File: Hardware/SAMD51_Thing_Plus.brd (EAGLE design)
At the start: 22.9 x 50.8 mm, 107 parts, among them J6 AMP FCI 10103594-0001LF, Q1 2.5A/30V, U1 MCP73831, U2 ATSAMD51J20A-A, U3 AP2112K-3.3V, U4 4MB Flash, Y1 32.768kHz

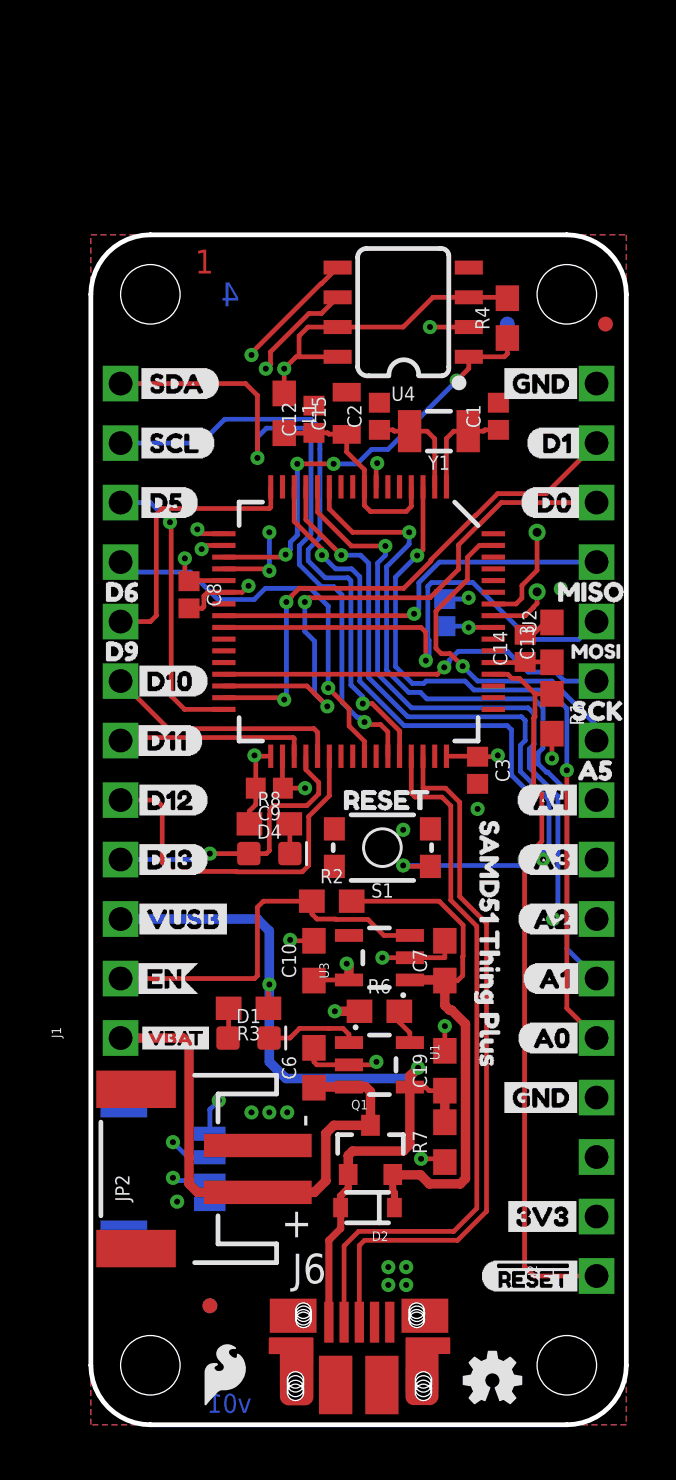
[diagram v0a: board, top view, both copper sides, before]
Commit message: Moving QWIIC connector, adding board name, moving bottom-placed capacitor to top
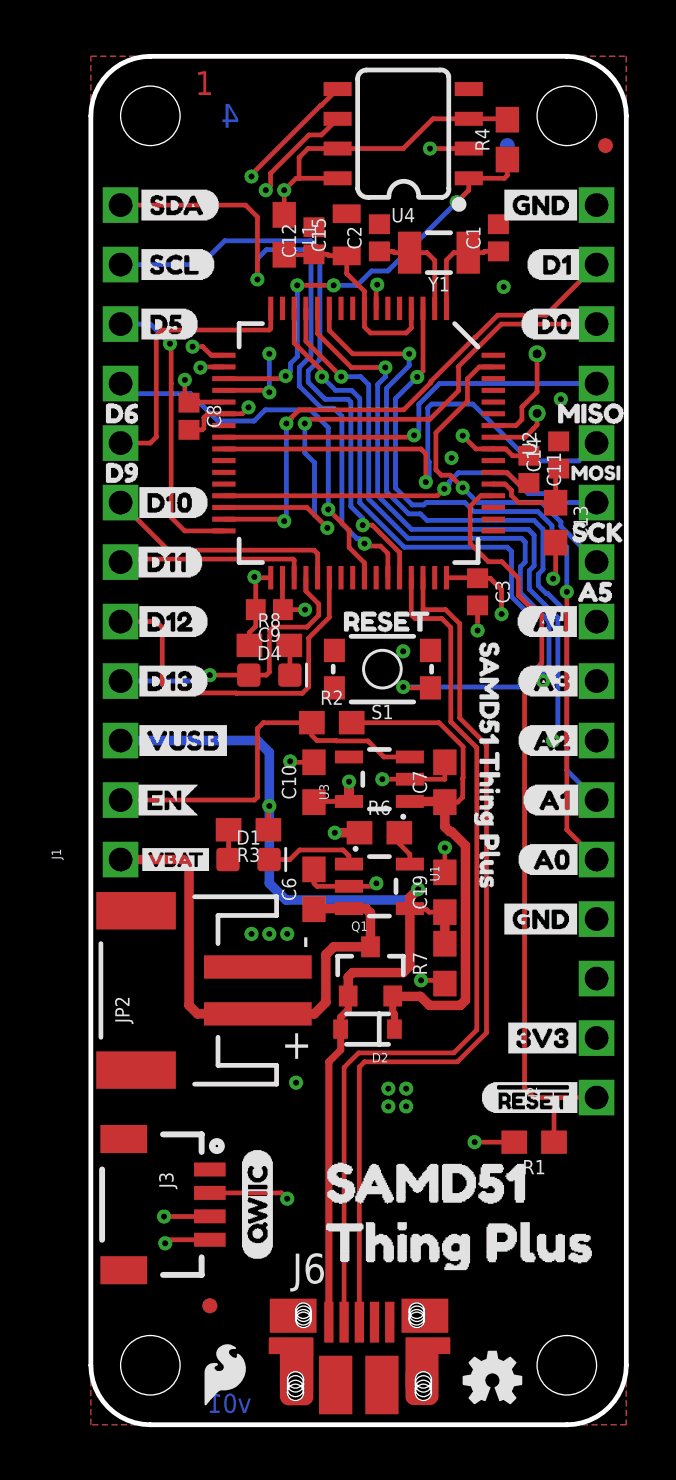
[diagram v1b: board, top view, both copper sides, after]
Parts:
- removed U$61: (no value), buzzard_labels (49):SAMD51_THING_PLUS0
- added U$63, U$65: (no value), buzzard_labels:SAMD510
- added U$64, U$66: (no value), buzzard_labels:THING_PLUS1
- moved R1 18.3 mm to (18.9, 12.1), turned to 180 degrees
- moved C14 8.38 mm to (20.0, 41.4)
- moved C1 7.62 mm to (17.4, 50.7)
- moved C2 7.62 mm to (12.3, 50.7)
- moved U$17 7.62 mm to (18.3, 47.0)
- moved U$18 7.62 mm to (18.5, 49.5)
- moved U$29 7.62 mm to (1.78, 47.0)
- moved U$30 7.62 mm to (1.78, 49.5)
- moved U$43 7.62 mm to (21.2, 44.5)
- moved U$44 7.62 mm to (21.2, 47.0)
- moved U$45 7.62 mm to (21.2, 49.5)
- moved U$48 7.62 mm to (5.97, 49.5)
- moved U$49 7.62 mm to (5.21, 47.0)
- moved U$50 7.62 mm to (5.21, 44.5)
- moved U4 7.62 mm to (13.3, 55.1)
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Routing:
- net SCL: track 55.9 -> 63.8 mm, vias 3 -> 2
- net D-: track 30.7 -> 38.3 mm
- net V_USB: track 36.6 -> 44.2 mm
- net D+: track 30.4 -> 38.0 mm
- net 3.3V: track 28.1 -> 33.3 mm
- net !RESET: track 37.5 -> 39.6 mm
- net VCC: track 2.52 -> 4.70 mm
- net GND: track 21.4 -> 23.4 mm, vias 21 -> 23
- net SDA: track 64.3 -> 62.6 mm
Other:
- board size 22.9 x 50.8 mm -> 22.9 x 58.4 mm

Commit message: updating version number
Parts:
- moved U$63 0.63 mm to (8.89, 9.53)
- moved U$64 0.63 mm to (8.89, 6.99)
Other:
- board text added: "Mike Hord and M. West"
- board text added: "v02"
- board text removed: "Mike Hord"
- board text removed: "v01"
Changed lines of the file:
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@@
 <setting verticaltext="up"/>
 </settings>
-<grid distance="0.00625" unitdist="inch" unit="inch" style="lines" multiple="1" display="yes" altdistance="0.001" altunitdist="inch" altunit="inch"/>
+<grid distance="0.0125" unitdist="inch" unit="inch" style="lines" multiple="1" display="yes" altdistance="0.005" altunitdist="inch" altunit="inch"/>
 <layers>
 <layer number="1" name="Top" color="4" fill="1" visible="yes" active="yes"/>
-<layer number="2" name="Route2" color="1" fill="3" visible="yes" active="yes"/>
-<layer number="15" name="Route15" color="4" fill="6" visible="yes" active="yes"/>
 <layer number="16" name="Bottom" color="1" fill="1" visible="yes" active="yes"/>
 <layer number="17" name="Pads" color="2" fill="1" visible="yes" active="yes"/>
@@
 <layer number="21" name="tPlace" color="16" fill="1" visible="yes" active="yes"/>
 <layer number="22" name="bPlace" color="14" fill="1" visible="yes" active="yes"/>
-<layer number="23" name="tOrigins" color="15" fill="1" visible="no" active="yes"/>
+<layer number="23" name="tOrigins" color="15" fill="1" visible="yes" active="yes"/>
 <layer number="24" name="bOrigins" color="15" fill="1" visible="yes" active="yes"/>
 <layer number="25" name="tNames" color="7" fill="1" visible="no" active="yes"/>
@@
 <layer number="31" name="tCream" color="7" fill="4" visible="no" active="yes"/>
 <layer number="32" name="bCream" color="7" fill="5" visible="no" active="yes"/>
+<layer number="33" name="tFinish" color="6" fill="3" visible="no" active="yes"/>
+<layer number="34" name="bFinish" color="6" fill="6" visible="no" active="yes"/>
+<layer number="35" name="tGlue" color="7" fill="4" visible="no" active="yes"/>
+<layer number="36" name="bGlue" color="7" fill="5" visible="no" active="yes"/>
+<layer number="37" name="tTest" color="7" fill="1" visible="no" active="yes"/>
+<layer number="38" name="bTest" color="7" fill="1" visible="no" active="yes"/>
 <layer number="39" name="tKeepout" color="4" fill="11" visible="no" active="yes"/>
-<layer number="40" name="bKeepout" color="1" fill="11" visible="yes" active="yes"/>
-<layer number="41" name="tRestrict" color="4" fill="10" visible="yes" active="yes"/>
-<layer number="42" name="bRestrict" color="1" fill="10" visible="yes" active="yes"/>
-<layer number="43" name="vRestrict" color="2" fill="10" visible="yes" active="yes"/>
+<layer number="40" name="bKeepout" color="1" fill="11" visible="no" active="yes"/>
+<layer number="41" name="tRestrict" color="4" fill="10" visible="no" active="yes"/>
+<layer number="42" name="bRestrict" color="1" fill="10" visible="no" active="yes"/>
+<layer number="43" name="vRestrict" color="2" fill="10" visible="no" active="yes"/>
 <layer number="44" name="Drills" color="7" fill="1" visible="no" active="yes"/>
-<layer number="45" name="Holes" color="7" fill="1" visible="no" active="yes"/>
+<layer number="45" name="Holes" color="7" fill="1" visible="yes" active="yes"/>
 <layer number="46" name="Milling" color="3" fill="1" visible="no" active="yes"/>
 <layer number="47" name="Measures" color="7" fill="1" visible="no" active="yes"/>
 <layer number="48" name="Document" color="7" fill="1" visible="no" active="yes"/>
 <layer number="49" name="Reference" color="7" fill="1" visible="no" active="yes"/>
-<layer number="51" name="tDocu" color="6" fill="1" visible="no" active="yes"/>
+<layer number="50" name="dxf" color="7" fill="1" visible="no" active="yes"/>
+<layer number="51" name="tDocu" color="6" fill="1" visible="yes" active="yes"/>
 <layer number="52" name="bDocu" color="7" fill="1" visible="no" active="yes"/>
+<layer number="91" name="Nets" color="2" fill="1" visible="no" active="no"/>
+<layer number="92" name="Busses" color="1" fill="1" visible="no" active="no"/>
+<layer number="93" name="Pins" color="2" fill="1" visible="no" active="no"/>
+<layer number="94" name="Symbols" color="4" fill="1" visible="no" active="no"/>
+<layer number="95" name="Names" color="7" fill="1" visible="no" active="no"/>
+<layer number="96" name="Values" color="7" fill="1" visible="no" active="no"/>
+<layer number="2" name="Route2" color="1" fill="3" visible="no" active="yes"/>
+<layer number="15" name="Route15" color="4" fill="6" visible="no" active="yes"/>
 <layer number="3" name="Route3" color="4" fill="3" visible="no" active="no"/>
 <layer number="4" name="Route4" color="1" fill="4" visible="no" active="no"/>
@@
 <layer number="13" name="Route13" color="4" fill="5" visible="no" active="no"/>
 <layer number="14" name="Route14" color="1" fill="6" visible="no" active="no"/>
-<layer number="33" name="tFinish" color="6" fill="3" visible="no" active="no"/>
-<layer number="34" name="bFinish" color="6" fill="6" visible="no" active="no"/>
-<layer number="35" name="tGlue" color="7" fill="4" visible="no" active="no"/>
-<layer number="36" name="bGlue" color="7" fill="5" visible="no" active="no"/>
-<layer number="37" name="tTest" color="7" fill="1" visible="no" active="no"/>
-<layer number="38" name="bTest" color="7" fill="1" visible="no" active="no"/>
-<layer number="50" name="dxf" color="7" fill="1" visible="no" active="no"/>
 <layer number="53" name="tGND_GNDA" color="7" fill="9" visible="no" active="no"/>
 <layer number="54" name="bGND_GNDA" color="1" fill="9" visible="no" active="no"/>
@@
 <layer number="89" name="SimProbes" color="9" fill="1" visible="no" active="no"/>
 <layer number="90" name="Modules" color="5" fill="1" visible="no" active="no"/>
-<layer number="91" name="Nets" color="2" fill="1" visible="no" active="no"/>
-<layer number="92" name="Busses" color="1" fill="1" visible="no" active="no"/>
-<layer number="93" name="Pins" color="2" fill="1" visible="no" active="no"/>
-<layer number="94" name="Symbols" color="4" fill="1" visible="no" active="no"/>
-<layer number="95" name="Names" color="7" fill="1" visible="no" active="no"/>
-<layer number="96" name="Values" color="7" fill="1" visible="no" active="no"/>
 <layer number="97" name="Info" color="7" fill="1" visible="no" active="no"/>
 <layer number="98" name="Guide" color="6" fill="1" visible="no" active="no"/>
@@
 <board>
 <plain>
-<text x="13.97" y="-19.05" size="1.778" layer="51" font="vector" ratio="15">Mike Hord</text>
+<text x="13.97" y="-19.05" size="1.778" layer="51" font="vector" ratio="15">Mike Hord and M. West</text>
 <text x="26.67" y="1.27" size="1.778" layer="47" font="vector" ratio="15">Units in inches</text>
 <wire x1="2.54" y1="58.42" x2="20.32" y2="58.42" width="0.2032" layer="20"/>
@@
 <text x="4.445" y="55.372" size="1.016" layer="15" font="vector" ratio="20">3</text>
 <text x="6.35" y="55.372" size="1.016" layer="16" font="vector" ratio="20" rot="MR0">4</text>
-<text x="6.858" y="0.508" size="0.8128" layer="16" font="vector" ratio="25" rot="MR0">v01</text>
+<text x="6.858" y="0.508" size="0.8128" layer="16" font="vector" ratio="25" rot="MR0">v02</text>
 <dimension x1="0" y1="58.42" x2="0" y2="0" x3="-13.97" y3="29.21" textsize="1.27" textratio="15" layer="47" dtype="vertical" unit="inch"/>
 <dimension x1="2.54" y1="55.88" x2="0" y2="0" x3="-11.43" y3="27.94" textsize="1.27" textratio="15" layer="47" dtype="vertical" unit="inch"/>
@@
 <element name="U$62" library="buzzard_labels (46)" package="QWIIC26" value="" x="7.112" y="6.985" rot="R90"/>
 <element name="U$60" library="buzzard_labels (50)" package="SAMD51_THING_PLUS0" value="" x="17.018" y="34.163" rot="R270"/>
-<element name="U$63" library="buzzard_labels" package="SAMD510" value="" x="8.89" y="10.16"/>
-<element name="U$64" library="buzzard_labels" package="THING_PLUS1" value="" x="8.89" y="7.62"/>
+<element name="U$63" library="buzzard_labels" package="SAMD510" value="" x="8.89" y="9.525"/>
+<element name="U$64" library="buzzard_labels" package="THING_PLUS1" value="" x="8.89" y="6.985"/>
 <element name="U$65" library="buzzard_labels" package="SAMD510" value="" x="23.01875" y="9.2075" rot="MR0"/>
 <element name="U$66" library="buzzard_labels" package="THING_PLUS1" value="" x="13.49375" y="9.36625" rot="MR0"/>

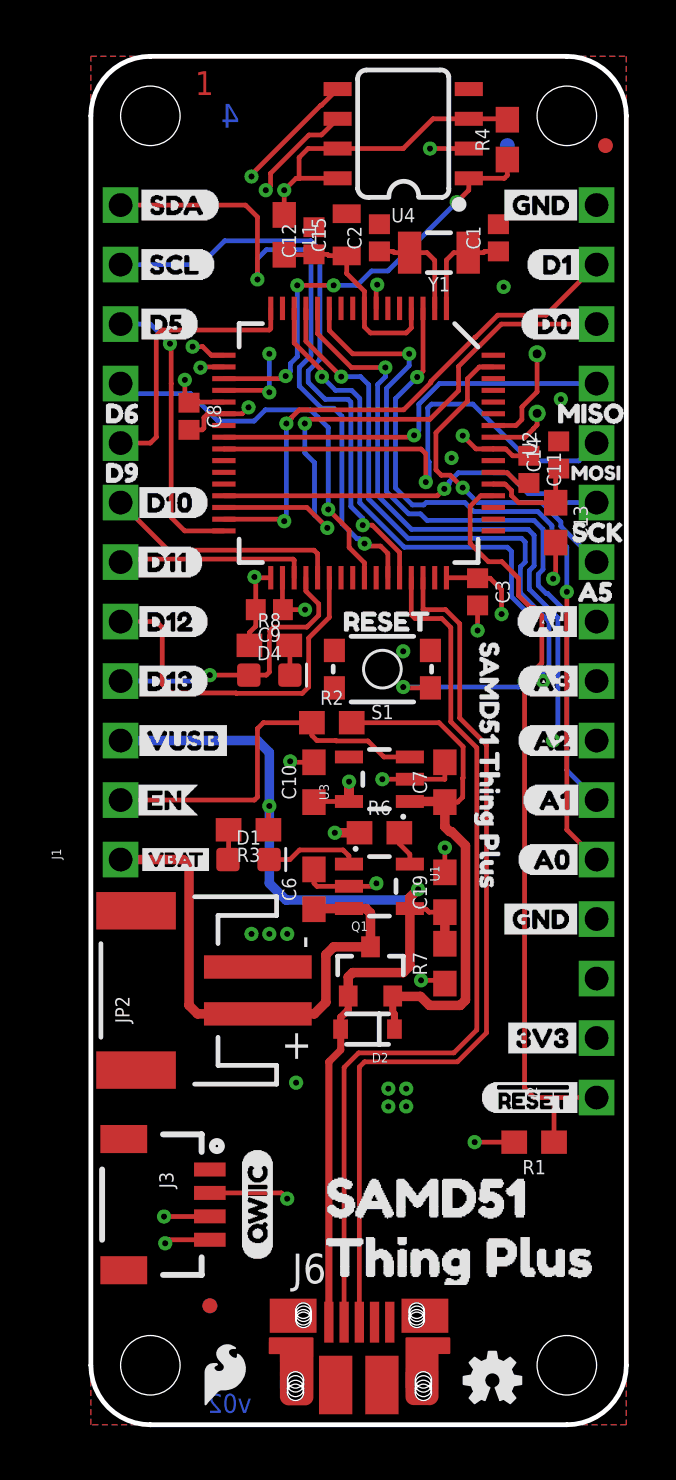
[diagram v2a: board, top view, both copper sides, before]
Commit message: connecting D4 to match feather footprint, removing short on USB connector
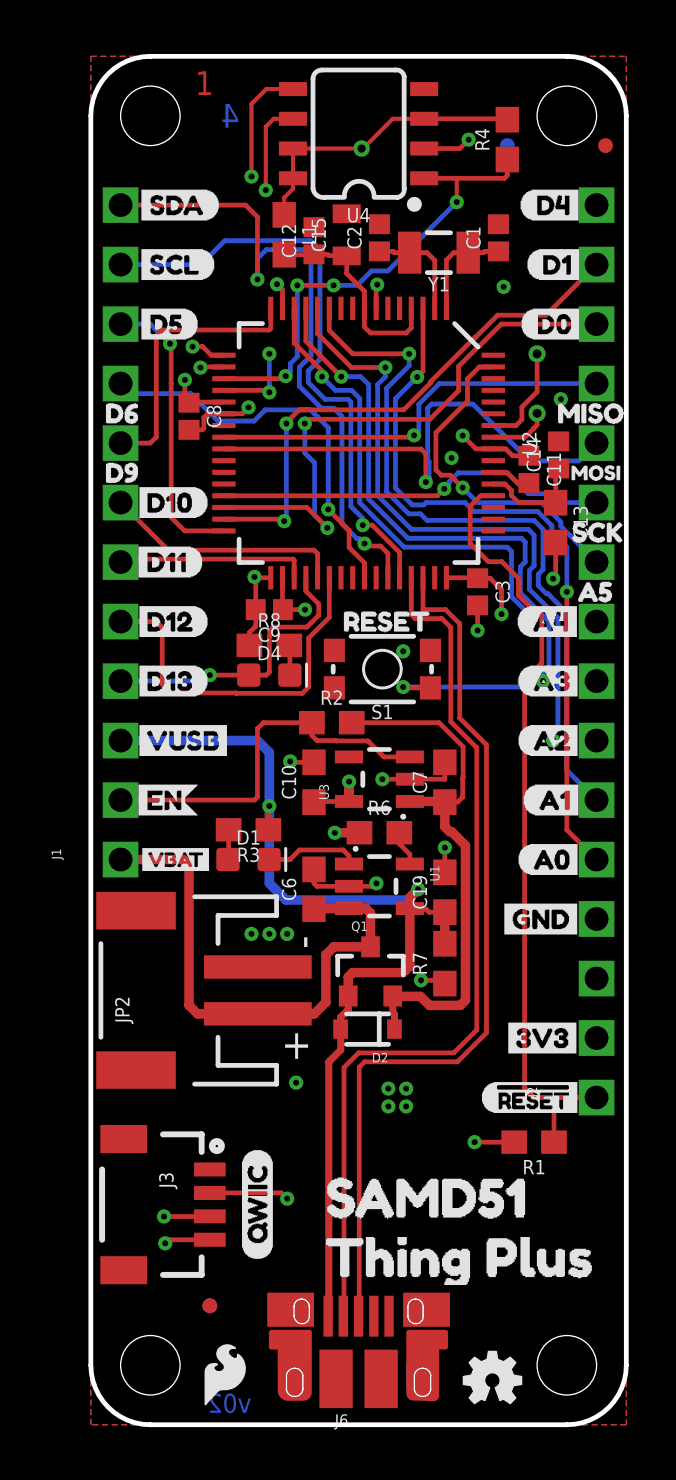
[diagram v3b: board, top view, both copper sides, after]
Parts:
- removed U$60: (no value), buzzard_labels (50):SAMD51_THING_PLUS0
- J6: device SparkFun-Connectors:USB-MICROB-PTH -> SparkFun-Connectors:USB-MICROB-PTH-MILL
- U$19: device buzzard_labels (44):GND12 -> buzzard_labels (28):D41
- U$46: device buzzard_labels (46):GND0 -> buzzard_labels (29):D41
- moved U4 1.91 mm to (11.4, 55.1)
- moved J6 1.59 mm to (11.4, 4.64)
- moved U$19 1.02 mm to (18.3, 52.1)
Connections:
- net D2_FLASH_MISO renamed FLASH_MISO
- net D3_FLASH_SCK renamed FLASH_SCK
- net D4_FLASH_MOSI renamed FLASH_MOSI
- removed net D8: U2.15
- new net D4: J2.16, U2.15
- net GND: no longer J2.16
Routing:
- net D4: track 0.00 -> 16.2 mm, vias 0 -> 1
- net FLASH_CS: track 18.6 -> 20.4 mm
- net FLASH_MISO: track 20.2 -> 21.7 mm
- net 3.3V: track 33.3 -> 32.6 mm
- net FLASH_SCK: track 15.2 -> 14.6 mm
- added copper zone on layer 15, net GND

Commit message: post checklist changes
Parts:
- removed JP2: LiPo, SparkFun-Connectors:JST-2-SMD
- added J4: (no value), SparkFun-Connectors:JST-2-SMD
- added JP1: JUMPER-SMT_3_2-NC_TRACE_SILK, SparkFun-Jumpers:SMT-JUMPER_3_2-NC_TRACE_SILK
- added R5, R9: 2.2k, SparkFun-Resistors:0603
- added U$60: (no value), buzzard_labels (30):NC0
- added U$61: (no value), buzzard_labels (30):NC1
- U$10: device buzzard_labels (44):A217 -> buzzard_labels (30):A26
- U$11: device buzzard_labels (44):A316 -> buzzard_labels (30):A37
- U$12: device buzzard_labels (44):A415 -> buzzard_labels (30):A48
- U$17: device buzzard_labels (44):D014 -> buzzard_labels (30):D09
- U$18: device buzzard_labels (44):D113 -> buzzard_labels (30):D110
- U$19: device buzzard_labels (28):D41 -> buzzard_labels (30):D411
- U$20: device buzzard_labels (44):GND20 -> buzzard_labels (30):GND3
- U$22: device buzzard_labels (44):EN11 -> buzzard_labels (33):EN0
- U$23: device buzzard_labels (44):VUSB9 -> buzzard_labels (33):VUSB2
- U$24: device buzzard_labels (44):D138 -> buzzard_labels (30):D1312
- U$25: device buzzard_labels (44):D127 -> buzzard_labels (37):D120
- U$26: device buzzard_labels (44):D116 -> buzzard_labels (30):D1113
- U$29: device buzzard_labels (44):D52 -> buzzard_labels (30):D515
- U$30: device buzzard_labels (44):SCL1 -> buzzard_labels (30):_SCL16
- U$32: device buzzard_labels (44):SDA0 -> buzzard_labels (30):_SDA17
- U$59: device buzzard_labels (44):D105 -> buzzard_labels (34):D100
- U$6: device buzzard_labels (44):#RESET22 -> buzzard_labels (38):#RESET0
- U$7: device buzzard_labels (44):3V321 -> buzzard_labels (30):3V32
- U$8: device buzzard_labels (44):A019 -> buzzard_labels (30):A04
- U$9: device buzzard_labels (44):A118 -> buzzard_labels (30):A15
- moved FD2 4.90 mm to (17.8, 57.1)
- moved U$65 2.73 mm to (23.0, 11.9)
- moved U$66 2.57 mm to (13.5, 11.9)
- moved U$52 2.54 mm to (5.46, 36.8)
- moved FD4 2.54 mm to (17.8, 57.1)
- moved U$53 2.54 mm to (5.84, 39.4)
- moved U$59 2.18 mm to (-0.13, 38.1)
- moved U$6 1.02 mm to (15.5, 14.0)
- moved U$7 0.76 mm to (16.6, 16.5)
- moved U$20 0.76 mm to (16.5, 21.6)
- moved U$11 0.64 mm to (17.5, 31.8)
- moved U$17 0.64 mm to (17.7, 47.0)
- moved U$19 0.64 mm to (17.7, 52.1)
- moved U$10 0.51 mm to (17.7, 29.2)
- moved U$12 0.51 mm to (17.7, 34.3)
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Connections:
- new net N$2: JP1.3, R5.2
- new net N$3: JP1.1, R9.2
- net 3.3V: now also JP1.2
- net GND: now also J4.1; no longer JP2.2
- net SCL: now also R5.1
- net SDA: now also R9.1
- net V_BATT: now also J4.2; no longer JP2.1
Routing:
- net MOSI: track 21.8 -> 16.0 mm
- net N$3: track 0.00 -> 5.37 mm, vias 0 -> 1
- net V_BATT: track 23.2 -> 19.0 mm
- net N$2: track 0.00 -> 3.38 mm, vias 0 -> 1
- net D0: track 24.5 -> 21.5 mm
- net SCL: track 63.8 -> 66.0 mm
- net A3: track 26.1 -> 24.0 mm
- net EN: track 16.4 -> 14.5 mm
- net A1: track 31.1 -> 29.4 mm
- net A2: track 28.8 -> 27.3 mm
- net A0: track 30.6 -> 29.3 mm
- net GND: track 23.4 -> 24.6 mm, vias 23 -> 26
- net A4: track 23.4 -> 22.4 mm
- net SDA: track 62.6 -> 63.6 mm
- net FLASH_MOSI: track 16.0 -> 15.2 mm
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- removed copper zone on layer 15, net GND
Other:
- board text added: "Mike Hord, Mary West & Andy England"
- board text added: "v03"
- board text removed: "Mike Hord and M. West"
- board text removed: "v02"
